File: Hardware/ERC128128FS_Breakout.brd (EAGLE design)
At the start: 30 x 16.8 mm, 19 parts, among them J1 ER-CON2.0-2P-SMD, J3 ER-CON31HT-1, U1 PMV160UP,215

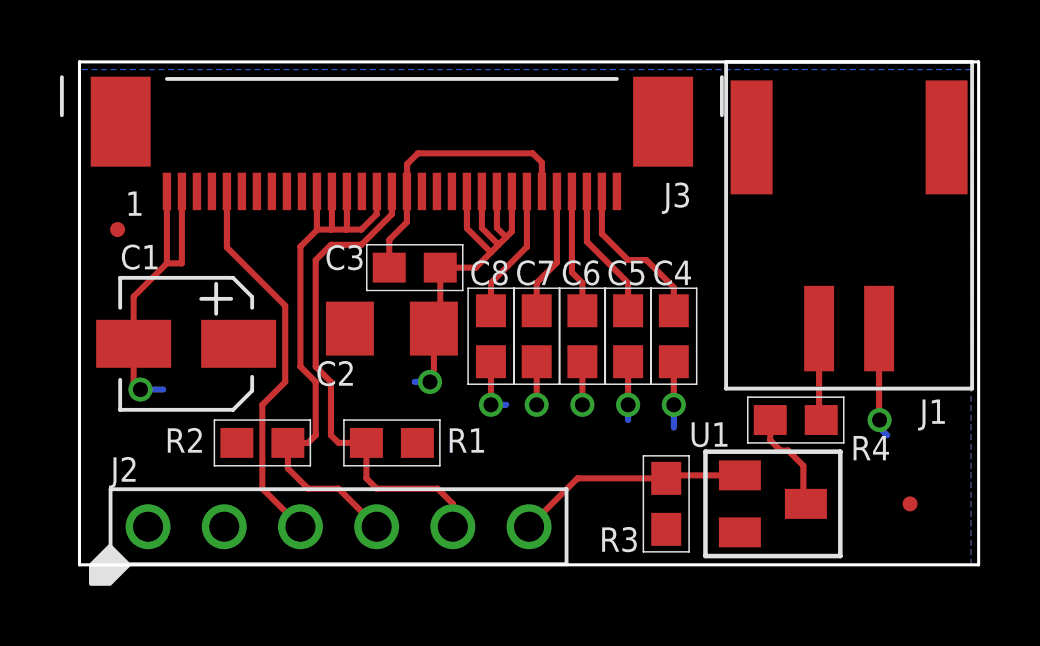
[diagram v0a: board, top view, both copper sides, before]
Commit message: Updated to new library style.
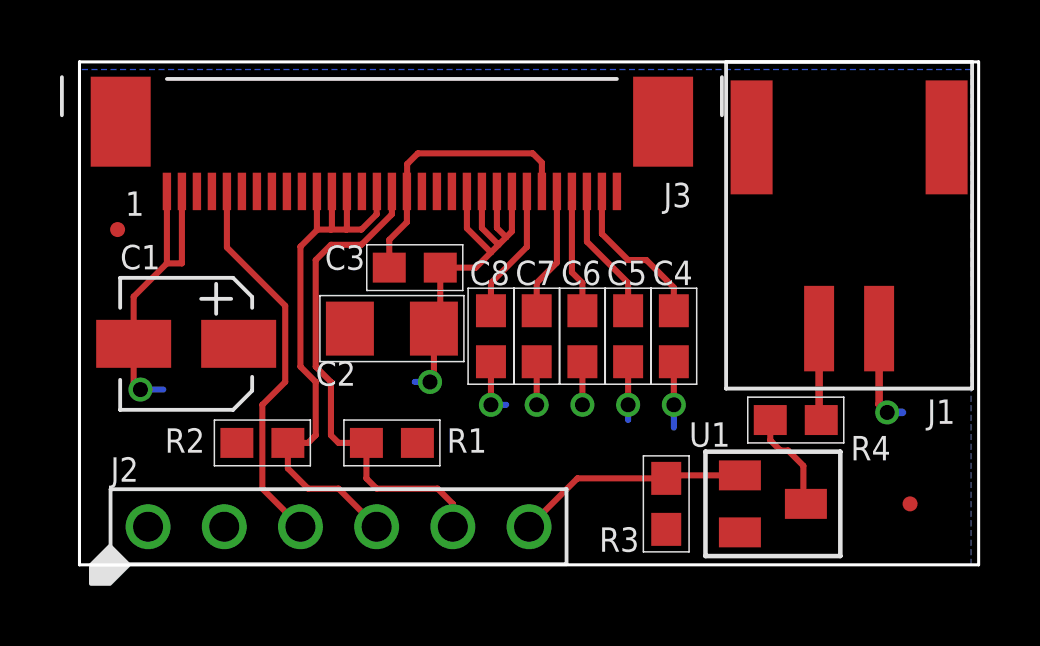
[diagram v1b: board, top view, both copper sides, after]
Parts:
- U1: device PP_DiscreteSemi:SOT-23 -> PP_DiscreteSemi:SOT-23-3
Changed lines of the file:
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@@
 <?xml version="1.0" encoding="utf-8"?>
 <!DOCTYPE eagle SYSTEM "eagle.dtd">
-<eagle version="6.5.0">
+<eagle version="6.6.0">
 <drawing>
 <settings>
@@
 </autorouter>
 <elements>
-<element name="J1" library="PP_Connectors" package="ER-CON2.0-2P-SMD" value="ER-CON2.0-2P-SMD" x="36.83" y="26.67" smashed="yes">
-<attribute name="NAME" x="39.18" y="23.495" size="0.8128" layer="25" font="vector" ratio="16"/>
-</element>
 <element name="J3" library="PP_Connectors" package="ER-CON31HT-1" value="ER-CON31HT-1" x="21.59" y="31.242" smashed="yes">
 <attribute name="LABEL03" value="PS2" x="45.72" y="7.112" size="1.778" layer="27" display="off"/>
@@
 <attribute name="NAME" x="30.64" y="30.714" size="0.8128" layer="25" font="vector" ratio="16"/>
 </element>
-<element name="U1" library="PP_DiscreteSemi" package="SOT-23" value="PMV160UP,215" x="34.29" y="20.828" smashed="yes" rot="R270">
+<element name="U1" library="PP_DiscreteSemi" package="SOT-23-3" value="PMV160UP,215" x="34.29" y="20.828" smashed="yes" rot="R270">
 <attribute name="NAME" x="31.496" y="22.733" size="0.8128" layer="25" font="vector" ratio="16"/>
 </element>
@@
 <element name="FID1" library="MF_Aesthetics" package="FIDUCIAL_0.5MM" value="FIDUCIAL_0.5MM" x="38.862" y="20.828"/>
 <element name="FID2" library="MF_Aesthetics" package="FIDUCIAL_0.5MM" value="FIDUCIAL_0.5MM" x="12.446" y="29.972"/>
+<element name="J1" library="PP_Connectors" package="ER-CON2.0-2P-SMD" value="ER-CON2.0-2P-SMD" x="36.83" y="26.67" smashed="yes">
+<attribute name="LABEL02" value="" x="37.83" y="23.67" size="0.8128" layer="21" font="vector" ratio="16" rot="R270" align="center-left"/>
+<attribute name="LABEL01" value="" x="35.83" y="23.67" size="0.8128" layer="21" font="vector" ratio="16" rot="R270" align="center-left"/>
+<attribute name="NAME" x="39.434" y="23.495" size="0.8128" layer="25" font="vector" ratio="16"/>
+</element>
 </elements>
 <signals>
 <signal name="GND">
-<contactref element="J1" pad="P$2"/>
 <contactref element="J3" pad="P$2"/>
 <contactref element="J3" pad="P$1"/>
@@
 <via x="30.988" y="24.13" extent="1-16" drill="0.5"/>
 <wire x1="30.988" y1="24.13" x2="30.988" y2="23.368" width="0.2032" layer="16"/>
-<wire x1="37.83" y1="26.67" x2="37.83" y2="23.638" width="0.2032" layer="1"/>
-<wire x1="37.83" y1="23.638" x2="37.846" y2="23.622" width="0.2032" layer="1"/>
-<via x="37.846" y="23.622" extent="1-16" drill="0.5"/>
-<wire x1="37.846" y1="23.622" x2="37.846" y2="23.368" width="0.2032" layer="16"/>
-<wire x1="37.846" y1="23.368" x2="38.1" y2="23.114" width="0.2032" layer="16"/>
+<contactref element="J1" pad="P$2"/>
+<wire x1="37.83" y1="26.67" x2="37.83" y2="24.146" width="0.254" layer="1"/>
+<wire x1="37.83" y1="24.146" x2="38.1" y2="23.876" width="0.254" layer="1"/>
+<via x="38.1" y="23.876" extent="1-16" drill="0.5"/>
+<wire x1="38.1" y1="23.876" x2="38.608" y2="23.876" width="0.254" layer="16"/>
 </signal>
 <signal name="3.3V">
@@
 </signal>
 <signal name="A">
-<contactref element="J1" pad="P$1"/>
 <contactref element="R4" pad="2"/>
 <wire x1="35.902" y1="23.622" x2="35.83" y2="23.694" width="0.254" layer="1"/>
-<wire x1="35.83" y1="23.694" x2="35.83" y2="26.67" width="0.2032" layer="1"/>
+<contactref element="J1" pad="P$1"/>
+<wire x1="35.83" y1="23.694" x2="35.83" y2="26.67" width="0.254" layer="1"/>
 </signal>
 <signal name="N$7">

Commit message: Basic Library complete.
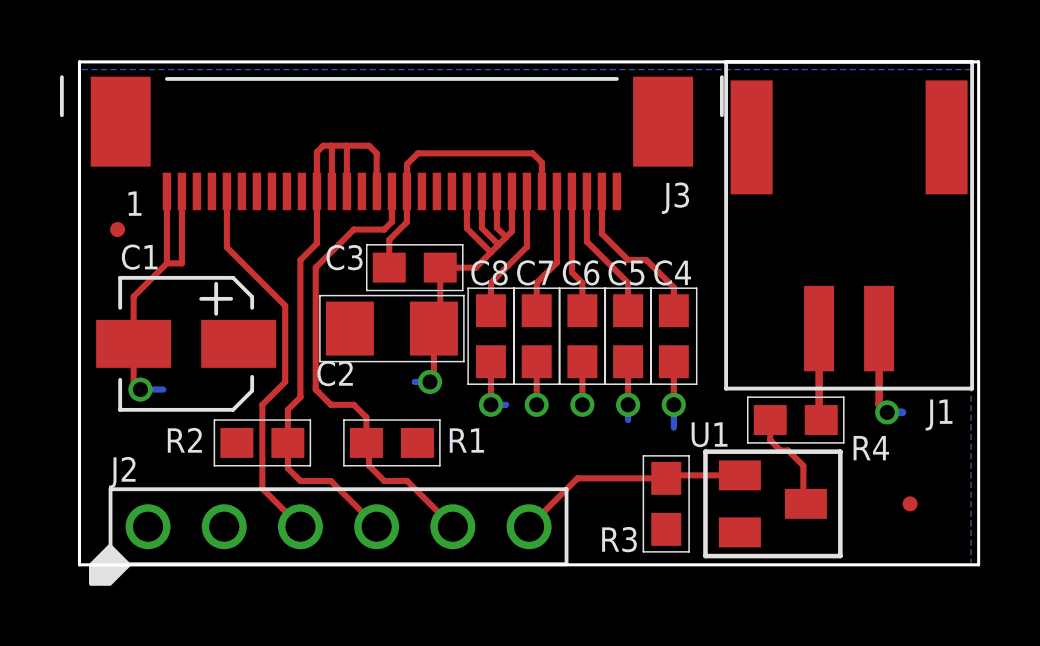
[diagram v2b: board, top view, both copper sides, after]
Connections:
- net LCD_SCL: now also J2.P$5, J3.P$16, R1.1; no longer J2.P$4, J3.P$11, J3.P$12, J3.P$13, J3.P$15, R2.1
- net LCD_SDA: now also J2.P$4, J3.P$11, J3.P$12, J3.P$13, J3.P$15, R2.1; no longer J2.P$5, J3.P$16, R1.1
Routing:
- net LCD_SDA: track 16.5 -> 21.2 mm
- net LCD_SCL: track 19.7 -> 15.6 mm
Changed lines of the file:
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@@
 <?xml version="1.0" encoding="utf-8"?>
 <!DOCTYPE eagle SYSTEM "eagle.dtd">
-<eagle version="6.6.0">
+<eagle version="7.4.0">
 <drawing>
 <settings>
@@
 <pass name="Default">
 <param name="RoutingGrid" value="50mil"/>
+<param name="AutoGrid" value="1"/>
+<param name="Efforts" value="0"/>
+<param name="TopRouterVariant" value="1"/>
 <param name="tpViaShape" value="round"/>
 <param name="PrefDir.1" value="|"/>
@@
 <attribute name="LABEL14" value="DB5" x="45.72" y="7.112" size="1.778" layer="27" display="off"/>
 <attribute name="LABEL30" value="V1" x="45.72" y="7.112" size="1.778" layer="27" display="off"/>
-<attribute name="LABEL15" value="DB6_SCL" x="45.72" y="7.112" size="1.778" layer="27" display="off"/>
+<attribute name="LABEL15" value="DB6_SDA" x="45.72" y="7.112" size="1.778" layer="27" display="off"/>
 <attribute name="LABEL31" value="V0" x="45.72" y="7.112" size="1.778" layer="27" display="off"/>
-<attribute name="LABEL16" value="DB7_SDA" x="45.72" y="7.112" size="1.778" layer="27" display="off"/>
+<attribute name="LABEL16" value="DB7_SCL" x="45.72" y="7.112" size="1.778" layer="27" display="off"/>
 <attribute name="LABEL17" value="VDD" x="45.72" y="7.112" size="1.778" layer="27" display="off"/>
 <attribute name="LABEL18" value="VDD" x="45.72" y="7.112" size="1.778" layer="27" display="off"/>
@@
 <element name="J2" library="MF_Connectors" package="PTH_2.54MM_01X06" value="" x="19.812" y="20.066" smashed="yes">
 <attribute name="LABEL02" value="LCD_RST" x="18.542" y="21.59" size="0.8128" layer="22" font="vector" ratio="16" rot="MR270" align="center-right"/>
-<attribute name="LABEL03" value="LCD_SCL" x="21.082" y="21.59" size="0.8128" layer="22" font="vector" ratio="16" rot="MR90" align="center-left"/>
-<attribute name="LABEL04" value="LCD_SDA" x="23.622" y="21.59" size="0.8128" layer="22" font="vector" ratio="16" rot="MR90" align="center-left"/>
+<attribute name="LABEL03" value="LCD_SDA" x="21.082" y="21.59" size="0.8128" layer="22" font="vector" ratio="16" rot="MR90" align="center-left"/>
+<attribute name="LABEL04" value="LCD_SCL" x="23.622" y="21.59" size="0.8128" layer="22" font="vector" ratio="16" rot="MR90" align="center-left"/>
 <attribute name="LABEL00" value="3.3V" x="13.462" y="21.59" size="0.8128" layer="22" font="vector" ratio="16" rot="MR90" align="center-left"/>
 <attribute name="LABEL01" value="GND" x="16.002" y="21.59" size="0.8128" layer="22" font="vector" ratio="16" rot="MR270" align="center-right"/>
@@
 <element name="U$1" library="PP_Aesthetics" package="LHE_FRAME" value="LHE_FRAME" x="40.132" y="28.956" rot="MR0">
 <attribute name="DNAME" value="Parker Dillmann" x="40.132" y="28.956" size="1.778" layer="28" rot="MR0" display="off"/>
-<attribute name="REVNUM" value="REV: 1" x="40.132" y="28.956" size="1.778" layer="28" rot="MR0" display="off"/>
+<attribute name="REVNUM" value="REV: 2" x="40.132" y="28.956" size="1.778" layer="28" rot="MR0" display="off"/>
 </element>
 <element name="FID1" library="MF_Aesthetics" package="FIDUCIAL_0.5MM" value="FIDUCIAL_0.5MM" x="38.862" y="20.828"/>
@@
 </signal>
 <signal name="LCD_SCL">
-<contactref element="J3" pad="P$15"/>
-<contactref element="R2" pad="1"/>
-<contactref element="J3" pad="P$11"/>
-<contactref element="J3" pad="P$12"/>
-<contactref element="J3" pad="P$13"/>
-<contactref element="J2" pad="P$4"/>
-<wire x1="21.082" y1="20.066" x2="19.812" y2="21.336" width="0.2032" layer="1"/>
-<wire x1="19.812" y1="21.336" x2="18.796" y2="21.336" width="0.2032" layer="1"/>
-<wire x1="18.796" y1="21.336" x2="18.122" y2="22.01" width="0.2032" layer="1"/>
-<wire x1="18.122" y1="22.01" x2="18.122" y2="22.86" width="0.2032" layer="1"/>
-<wire x1="18.122" y1="22.86" x2="18.796" y2="22.86" width="0.2032" layer="1"/>
-<wire x1="18.796" y1="22.86" x2="19.05" y2="23.114" width="0.2032" layer="1"/>
-<wire x1="19.05" y1="23.114" x2="19.05" y2="24.892" width="0.2032" layer="1"/>
-<wire x1="19.05" y1="24.892" x2="18.542" y2="25.4" width="0.2032" layer="1"/>
-<wire x1="18.542" y1="25.4" x2="18.542" y2="29.404040625" width="0.2032" layer="1"/>
-<wire x1="18.542" y1="29.404040625" x2="19.109959375" y2="29.972" width="0.2032" layer="1"/>
-<wire x1="19.109959375" y1="29.972" x2="19.558" y2="29.972" width="0.2032" layer="1"/>
-<wire x1="19.558" y1="29.972" x2="20.066" y2="29.972" width="0.2032" layer="1"/>
-<wire x1="20.066" y1="29.972" x2="20.574" y2="29.972" width="0.2032" layer="1"/>
-<wire x1="20.574" y1="29.972" x2="21.082" y2="30.48" width="0.2032" layer="1"/>
-<wire x1="21.082" y1="30.48" x2="21.082" y2="31.234" width="0.2032" layer="1"/>
-<wire x1="21.082" y1="31.234" x2="21.09" y2="31.242" width="0.2032" layer="1"/>
-<wire x1="19.09" y1="31.242" x2="19.09" y2="29.991959375" width="0.2032" layer="1"/>
-<wire x1="19.09" y1="29.991959375" x2="19.109959375" y2="29.972" width="0.2032" layer="1"/>
-<wire x1="19.59" y1="31.242" x2="19.59" y2="30.004" width="0.2032" layer="1"/>
-<wire x1="19.59" y1="30.004" x2="19.558" y2="29.972" width="0.2032" layer="1"/>
-<wire x1="20.09" y1="31.242" x2="20.09" y2="29.996" width="0.2032" layer="1"/>
-<wire x1="20.09" y1="29.996" x2="20.066" y2="29.972" width="0.2032" layer="1"/>
+<contactref element="R1" pad="1"/>
+<contactref element="J3" pad="P$16"/>
+<contactref element="J2" pad="P$5"/>
+<wire x1="21.59" y1="31.242" x2="21.59" y2="30.226" width="0.2032" layer="1"/>
+<wire x1="21.59" y1="30.226" x2="21.336" y2="29.972" width="0.2032" layer="1"/>
+<wire x1="21.336" y1="29.972" x2="20.32" y2="29.972" width="0.2032" layer="1"/>
+<wire x1="20.32" y1="29.972" x2="19.05" y2="28.702" width="0.2032" layer="1"/>
+<wire x1="19.05" y1="28.702" x2="19.05" y2="24.638" width="0.2032" layer="1"/>
+<wire x1="19.05" y1="24.638" x2="19.558" y2="24.13" width="0.2032" layer="1"/>
+<wire x1="19.558" y1="24.13" x2="20.32" y2="24.13" width="0.2032" layer="1"/>
+<wire x1="20.32" y1="24.13" x2="20.74" y2="23.71" width="0.2032" layer="1"/>
+<wire x1="20.74" y1="23.71" x2="20.74" y2="22.86" width="0.2032" layer="1"/>
+<wire x1="20.74" y1="22.86" x2="20.828" y2="22.772" width="0.2032" layer="1"/>
+<wire x1="20.828" y1="22.772" x2="20.828" y2="22.098" width="0.2032" layer="1"/>
+<wire x1="20.828" y1="22.098" x2="21.336" y2="21.59" width="0.2032" layer="1"/>
+<wire x1="21.336" y1="21.59" x2="22.098" y2="21.59" width="0.2032" layer="1"/>
+<wire x1="22.098" y1="21.59" x2="23.622" y2="20.066" width="0.2032" layer="1"/>
 </signal>
 <signal name="LCD_SDA">
-<contactref element="J3" pad="P$16"/>
-<contactref element="R1" pad="1"/>
-<contactref element="J2" pad="P$5"/>
-<wire x1="23.622" y1="20.066" x2="23.622" y2="20.828" width="0.2032" layer="1"/>
-<wire x1="23.622" y1="20.828" x2="23.114" y2="21.336" width="0.2032" layer="1"/>
-<wire x1="23.114" y1="21.336" x2="21.082" y2="21.336" width="0.2032" layer="1"/>
-<wire x1="21.082" y1="21.336" x2="20.74" y2="21.678" width="0.2032" layer="1"/>
-<wire x1="20.74" y1="21.678" x2="20.74" y2="22.86" width="0.2032" layer="1"/>
-<wire x1="20.74" y1="22.86" x2="19.812" y2="22.86" width="0.2032" layer="1"/>
-<wire x1="19.812" y1="22.86" x2="19.558" y2="23.114" width="0.2032" layer="1"/>
-<wire x1="19.558" y1="23.114" x2="19.558" y2="24.892" width="0.2032" layer="1"/>
-<wire x1="19.558" y1="24.892" x2="19.05" y2="25.4" width="0.2032" layer="1"/>
-<wire x1="19.05" y1="25.4" x2="19.05" y2="28.956" width="0.2032" layer="1"/>
-<wire x1="19.05" y1="28.956" x2="19.558" y2="29.464" width="0.2032" layer="1"/>
-<wire x1="19.558" y1="29.464" x2="20.574" y2="29.464" width="0.2032" layer="1"/>
-<wire x1="20.574" y1="29.464" x2="21.59" y2="30.48" width="0.2032" layer="1"/>
-<wire x1="21.59" y1="30.48" x2="21.59" y2="31.242" width="0.2032" layer="1"/>
+<contactref element="J3" pad="P$13"/>
+<contactref element="J3" pad="P$11"/>
+<contactref element="R2" pad="1"/>
+<contactref element="J3" pad="P$12"/>
+<contactref element="J3" pad="P$15"/>
+<contactref element="J2" pad="P$4"/>
+<wire x1="19.09" y1="31.242" x2="19.09" y2="29.504" width="0.2032" layer="1"/>
+<wire x1="19.09" y1="29.504" x2="18.542" y2="28.956" width="0.2032" layer="1"/>
+<wire x1="18.542" y1="28.956" x2="18.542" y2="24.384" width="0.2032" layer="1"/>
+<wire x1="18.542" y1="24.384" x2="18.122" y2="23.964" width="0.2032" layer="1"/>
+<wire x1="18.122" y1="23.964" x2="18.122" y2="22.86" width="0.2032" layer="1"/>
+<wire x1="18.122" y1="22.86" x2="18.122" y2="22.01" width="0.2032" layer="1"/>
+<wire x1="18.122" y1="22.01" x2="18.542" y2="21.59" width="0.2032" layer="1"/>
+<wire x1="18.542" y1="21.59" x2="19.558" y2="21.59" width="0.2032" layer="1"/>
+<wire x1="19.558" y1="21.59" x2="21.082" y2="20.066" width="0.2032" layer="1"/>
+<wire x1="19.09" y1="31.242" x2="19.09" y2="32.552" width="0.2032" layer="1"/>
+<wire x1="19.09" y1="32.552" x2="19.304" y2="32.766" width="0.2032" layer="1"/>
+<wire x1="19.304" y1="32.766" x2="19.558" y2="32.766" width="0.2032" layer="1"/>
+<wire x1="19.558" y1="32.766" x2="20.066" y2="32.766" width="0.2032" layer="1"/>
+<wire x1="20.066" y1="32.766" x2="20.828" y2="32.766" width="0.2032" layer="1"/>
+<wire x1="20.828" y1="32.766" x2="21.082" y2="32.512" width="0.2032" layer="1"/>
+<wire x1="21.082" y1="32.512" x2="21.082" y2="31.25" width="0.2032" layer="1"/>
+<wire x1="21.082" y1="31.25" x2="21.09" y2="31.242" width="0.2032" layer="1"/>
+<wire x1="19.59" y1="31.242" x2="19.59" y2="32.734" width="0.2032" layer="1"/>
+<wire x1="19.59" y1="32.734" x2="19.558" y2="32.766" width="0.2032" layer="1"/>
+<wire x1="20.09" y1="31.242" x2="20.09" y2="32.742" width="0.2032" layer="1"/>
+<wire x1="20.09" y1="32.742" x2="20.066" y2="32.766" width="0.2032" layer="1"/>
 </signal>
 <signal name="LCD_RST">
